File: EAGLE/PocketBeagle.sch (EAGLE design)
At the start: 50 parts, among them U1 OSD3358-512M-BSM, U2 SN74LVC1G07DCK, U3 TPD4S012DRY, X1 10118192-0001LF, X2 MICROSD, Y1 24 MHz

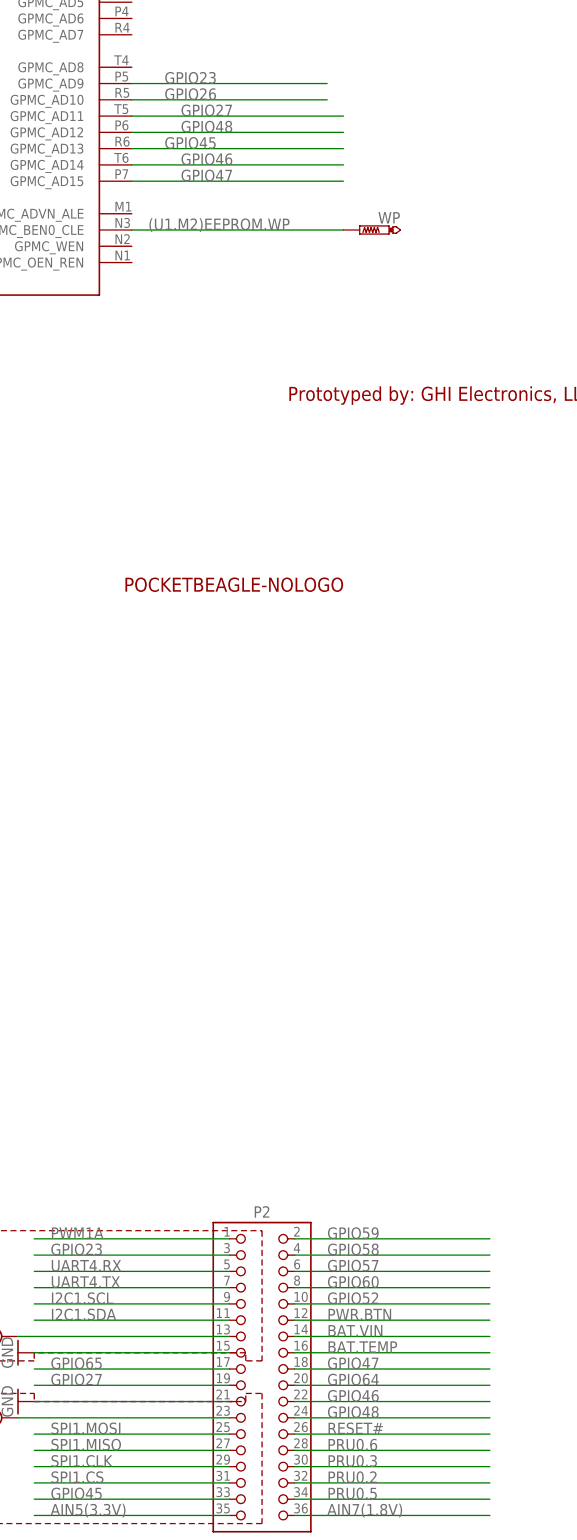
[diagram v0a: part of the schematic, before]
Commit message: Update P2_24 signal name
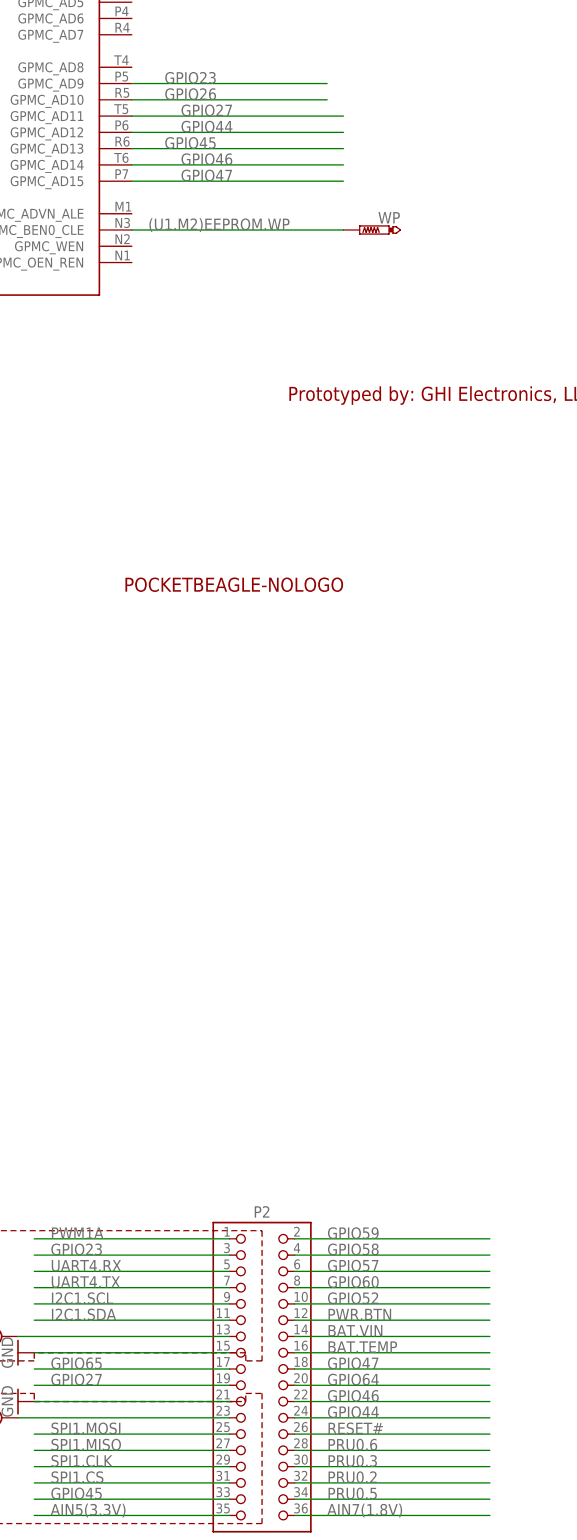
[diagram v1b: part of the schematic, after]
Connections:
- net GPIO48 renamed GPIO44
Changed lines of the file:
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@@
 <?xml version="1.0" encoding="utf-8"?>
 <!DOCTYPE eagle SYSTEM "eagle.dtd">
-<eagle version="7.7.0">
+<eagle version="8.3.1">
 <drawing>
 <settings>
 <setting alwaysvectorfont="no"/>
+<setting keepoldvectorfont="yes"/>
 <setting verticaltext="up"/>
 </settings>
@@
 </segment>
 </net>
-<net name="GPIO48" class="0">
+<net name="GPIO44" class="0">
 <segment>
 <wire x1="805.18" y1="101.6" x2="774.7" y2="101.6" width="0.1524" layer="91"/>

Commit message: Add rev A2b files
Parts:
- removed C4: .1uF, 6.3V, GHI-BasicComponents:CAPACITOR-(INCH)-0402
- removed U3: TPD4S012DRY, GHI-IC:TPD4S012DRYR
- added D1, D2, D3, D4: (no value), Discrete-new:D-ESD-2P-DOUBLE
- C2, C3: value 18pF, 50V -> 22pF, 50V
- Y1: value 24 MHz -> 24 MHz 20pF
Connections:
- net (U1.K14)USBC.ID: now also D4.2; no longer U3.ID
- net (U1.K15)USBC.D+: now also D1.2; no longer U3.D+
- net (U1.K16)USBC.D-: now also D2.2; no longer U3.D-
- net GND: now also D1.1, D2.1, D3.1, D4.1; no longer C4.2, U3.GND
- net VIN.USB: now also D3.2; no longer C4.1, U3.VBUS
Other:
- note added: "06/10/2021"
- note added: "1.Changed C2,C3 from 18pF to 22pF. 2.Changed Y1 from 24MHz_18pF to 24MHz_22pF. 3.Use ESD discrete devices(D1-D4) to replace U3 4.Changed U2 from SN74LVC1G07DCKR to 74LVC1G07GV,125. 5.The PCB Revision for this board is Rev A2b."
- note added: "A2b"
- note added: "FJN"
